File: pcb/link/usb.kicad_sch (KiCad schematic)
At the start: 40 parts, among them J14 68021-204HLF, J19 USB4105-GF-A, U10 TPS2021D, U2 CAHCT1G14QDBVRQ1, U6 USB3340-EZK-TR, U7 ADG772BCPZ-1REEL, Y2 ECS-2520SMV-240-FP-TR

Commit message: remove 3V3VREF TP (and upgrade to kicad 10) (closes #105)
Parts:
- removed TP5: 3.3V ULPI, TestPoint:TestPoint_Pad_1.0x1.0mm, symbol Connector:TestPoint

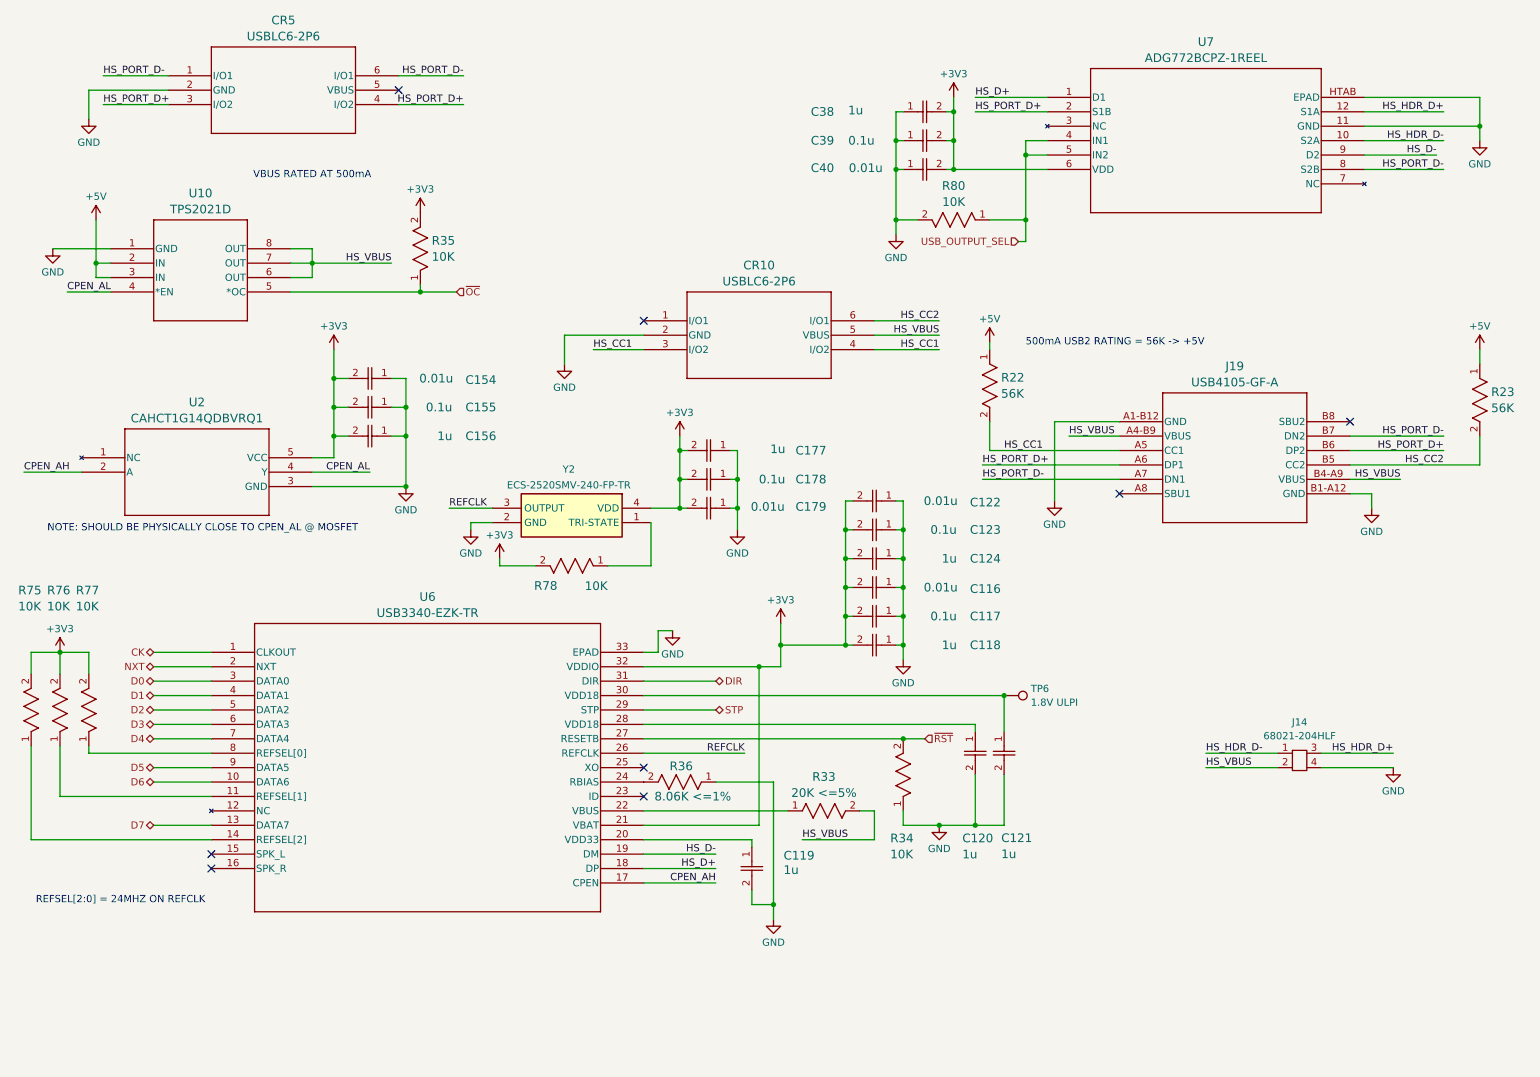
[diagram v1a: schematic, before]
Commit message: add filtering caps on TPS gates (closes #107)
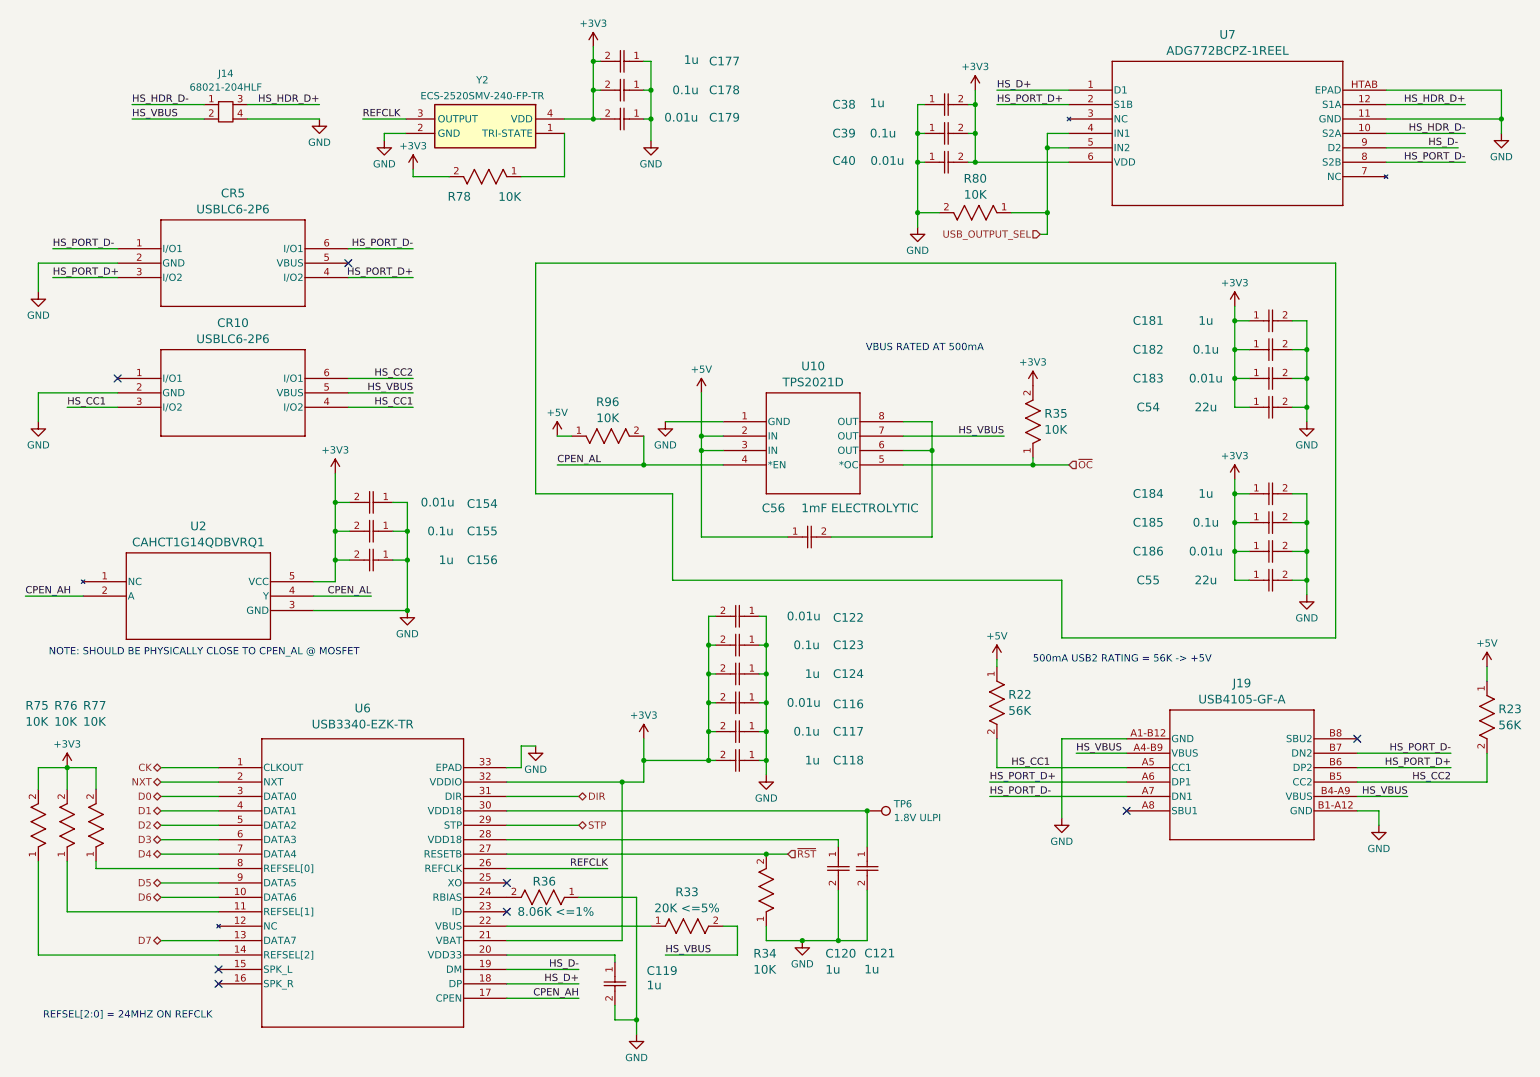
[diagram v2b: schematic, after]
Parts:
- added C181, C184: 1u, OroLink:cap_UMK105 CG080CV-F_TAY, symbol OroLink:JMK105BJ105KVHF
- added C182, C185: 0.1u, OroLink:CAP_MSAS1L-3_TAY, symbol OroLink:MSAST1L3YB5104KFNA01
- added C183, C186: 0.01u, OroLink:CAP_0402_N_WAL, symbol OroLink:0402B103J160CT
- added C54, C55: 22u, OroLink:CAP_CM05_K_KAV, symbol OroLink:CM05X5R226M06AH080
- added C56: 1mF ELECTROLYTIC, OroLink:CAP_99614E3_VIS, symbol OroLink:MAL215099614E3
- added R96: 10K, OroLink:STA_RMCF0402_STP, symbol OroLink:RMCF0402FT10K0
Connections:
- net +3V3: now also C181.1, C182.1, C183.1, C184.1, C185.1, C186.1, C54.1, C55.1
- net +5V: now also C56.1, R96.1
- net CPEN_AL: now also R96.2
- net GND: now also C181.2, C182.2, C183.2, C184.2, C185.2, C186.2, C54.2, C55.2
- net HS_VBUS: no longer U10.6 (OUT), U10.8 (OUT)
- new net: C56.2, U10.6 (OUT), U10.8 (OUT)
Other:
- moved on the sheet: C116, C117, C118, C119, C120, C121, C122, C123, C124, C154, C155, C156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
